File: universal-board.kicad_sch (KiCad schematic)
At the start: 48 parts, among them J1 USB_C_Receptacle, J2 Conn_02x04_Odd_Even, J3 Conn_01x08, J4 CONN_WS2812, J5 CONN_I2C_GROVE, J6 CONN_UART, Q1 BSS138, SW1 SW_RESET, SW2 SW_ACK, U1 USBLC6-2SC6, U2 AMS1117-3.3, U3 CH224K, U4 USBLC6-2SC6, U5 74AHCT1G125, U6 TSOP384xx, U7 ESP32-S3-WROOM-1-N16

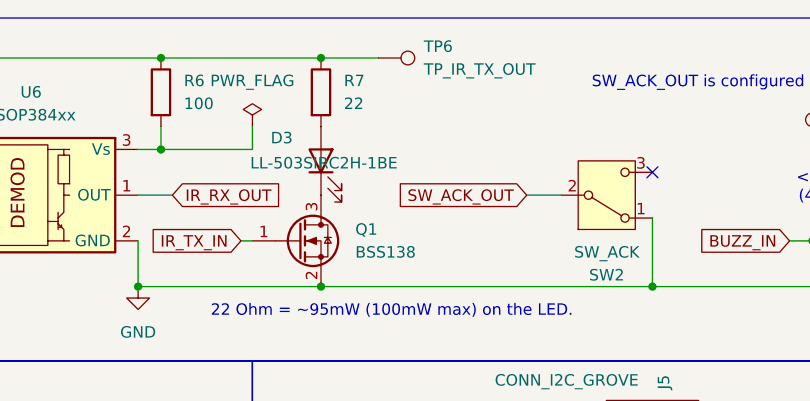
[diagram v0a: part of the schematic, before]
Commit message: PCB is routed, but needs more work.
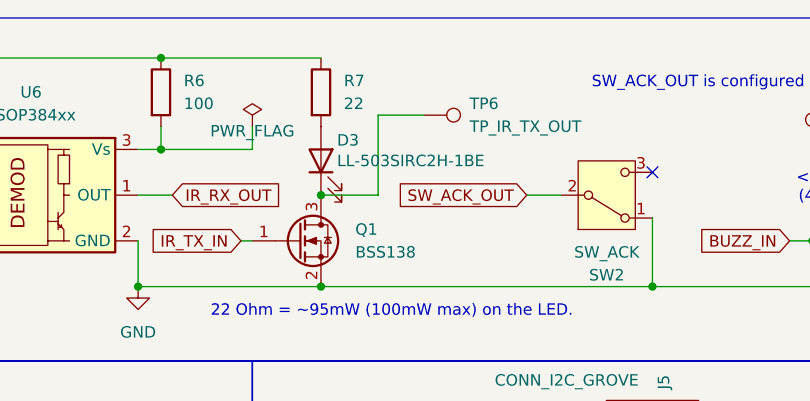
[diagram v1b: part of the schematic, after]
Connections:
- net 3.3V: no longer TP6.1
- net at D3.1 (K), Q1.3 (D): now also TP6.1
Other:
- moved on the sheet: TP6
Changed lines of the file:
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@@
 	)
 	(junction
+		(at 199.39 31.75)
+		(diameter 0)
+		(color 0 0 0 0)
+	)
+	(junction
 		(at 59.69 190.5)
 		(diameter 0)
@@
 	)
 	(junction
-		(at 199.39 16.51)
-		(diameter 0)
-		(color 0 0 0 0)
-	)
-	(junction
 		(at 46.99 190.5)
 		(diameter 0)
@@
 	(wire
 		(pts
+			(xy 205.74 22.86) (xy 210.82 22.86)
+		)
+		(stroke
+			(width 0)
+			(type default)
+		)
+	)
+	(wire
+		(pts
 			(xy 260.35 82.55) (xy 260.35 99.06)
 		)
@@
 	(wire
 		(pts
-			(xy 199.39 16.51) (xy 205.74 16.51)
-		)
-		(stroke
-			(width 0)
-			(type default)
-		)
-	)
-	(wire
-		(pts
 			(xy 97.79 121.92) (xy 135.89 121.92)
 		)
@@
 	(wire
 		(pts
+			(xy 205.74 31.75) (xy 199.39 31.75)
+		)
+		(stroke
+			(width 0)
+			(type default)
+		)
+	)
+	(wire
+		(pts
 			(xy 127 90.17) (xy 114.3 90.17)
 		)
@@
 	(wire
 		(pts
+			(xy 205.74 22.86) (xy 205.74 31.75)
+		)
+		(stroke
+			(width 0)
+			(type default)
+		)
+	)
+	(wire
+		(pts
 			(xy 171.45 63.5) (xy 154.94 63.5)
 		)
@@
 		(on_board yes)
 		(dnp no)
-		(fields_autoplaced yes)
 		(property "Reference" "#FLG04"
 			(at 191.77 22.225 0)
@@
 		)
 		(property "Value" "PWR_FLAG"
-			(at 191.77 19.05 0)
+			(at 191.77 24.638 0)
 			(effects
 				(font
@@
 		(dnp no)
 		(property "Reference" "D3"
-			(at 193.802 25.4 90)
+			(at 201.168 25.654 90)
 			(effects
 				(font
@@
 		)
 		(property "Value" "LL-503SIRC2H-1BE"
-			(at 191.516 28.194 90)
+			(at 201.168 27.94 90)
 			(effects
 				(font
@@
 	(symbol
 		(lib_id "Connector:TestPoint")
-		(at 205.74 16.51 270)
+		(at 210.82 22.86 270)
 		(unit 1)
 		(exclude_from_sim no)
@@
 		(fields_autoplaced yes)
 		(property "Reference" "TP6"
-			(at 210.82 15.2399 90)
+			(at 215.9 21.5899 90)
 			(effects
 				(font
@@
 		)
 		(property "Value" "TP_IR_TX_OUT"
-			(at 210.82 17.7799 90)
+			(at 215.9 24.1299 90)
 			(effects
 				(font
@@
 		)
 		(property "Footprint" "TestPoint:TestPoint_Pad_D2.0mm"
-			(at 205.74 21.59 0)
+			(at 210.82 27.94 0)
 			(effects
 				(font
@@
 		)
 		(property "Datasheet" "~"
-			(at 205.74 21.59 0)
+			(at 210.82 27.94 0)
 			(effects
 				(font
@@
 		)
 		(property "Description" "test point"
-			(at 205.74 16.51 0)
+			(at 210.82 22.86 0)
 			(effects
 				(font

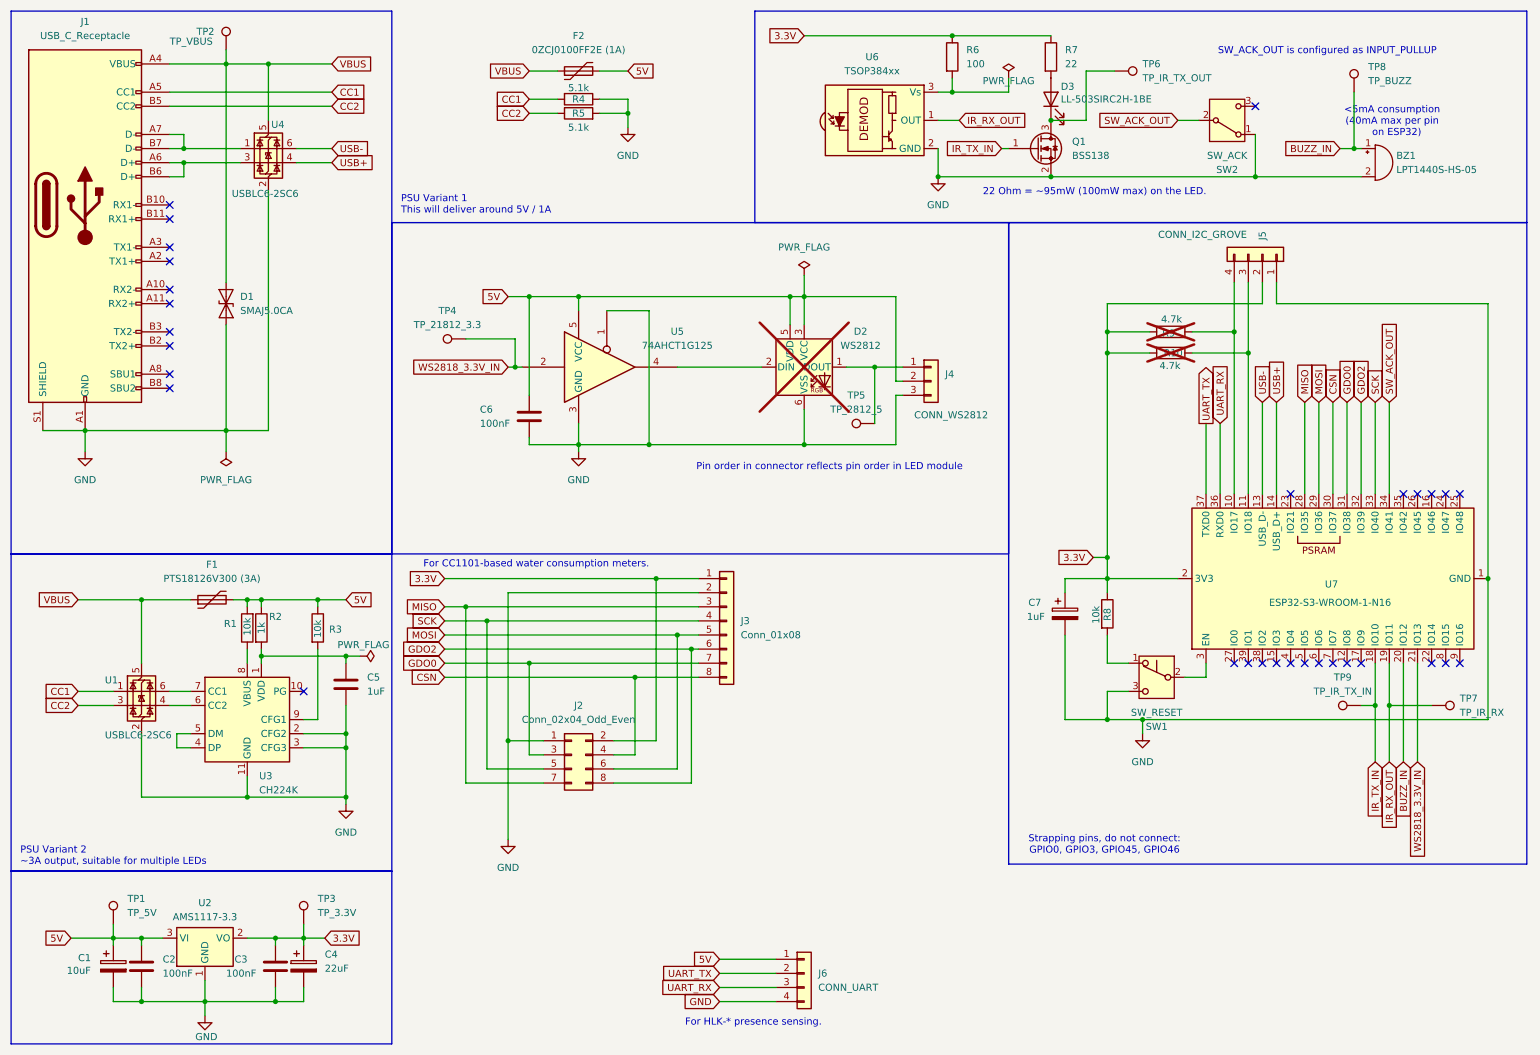
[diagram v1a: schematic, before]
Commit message: Prep for rev 3:
- removed 3A PSU
- added 2 33 ohm resistors for USB
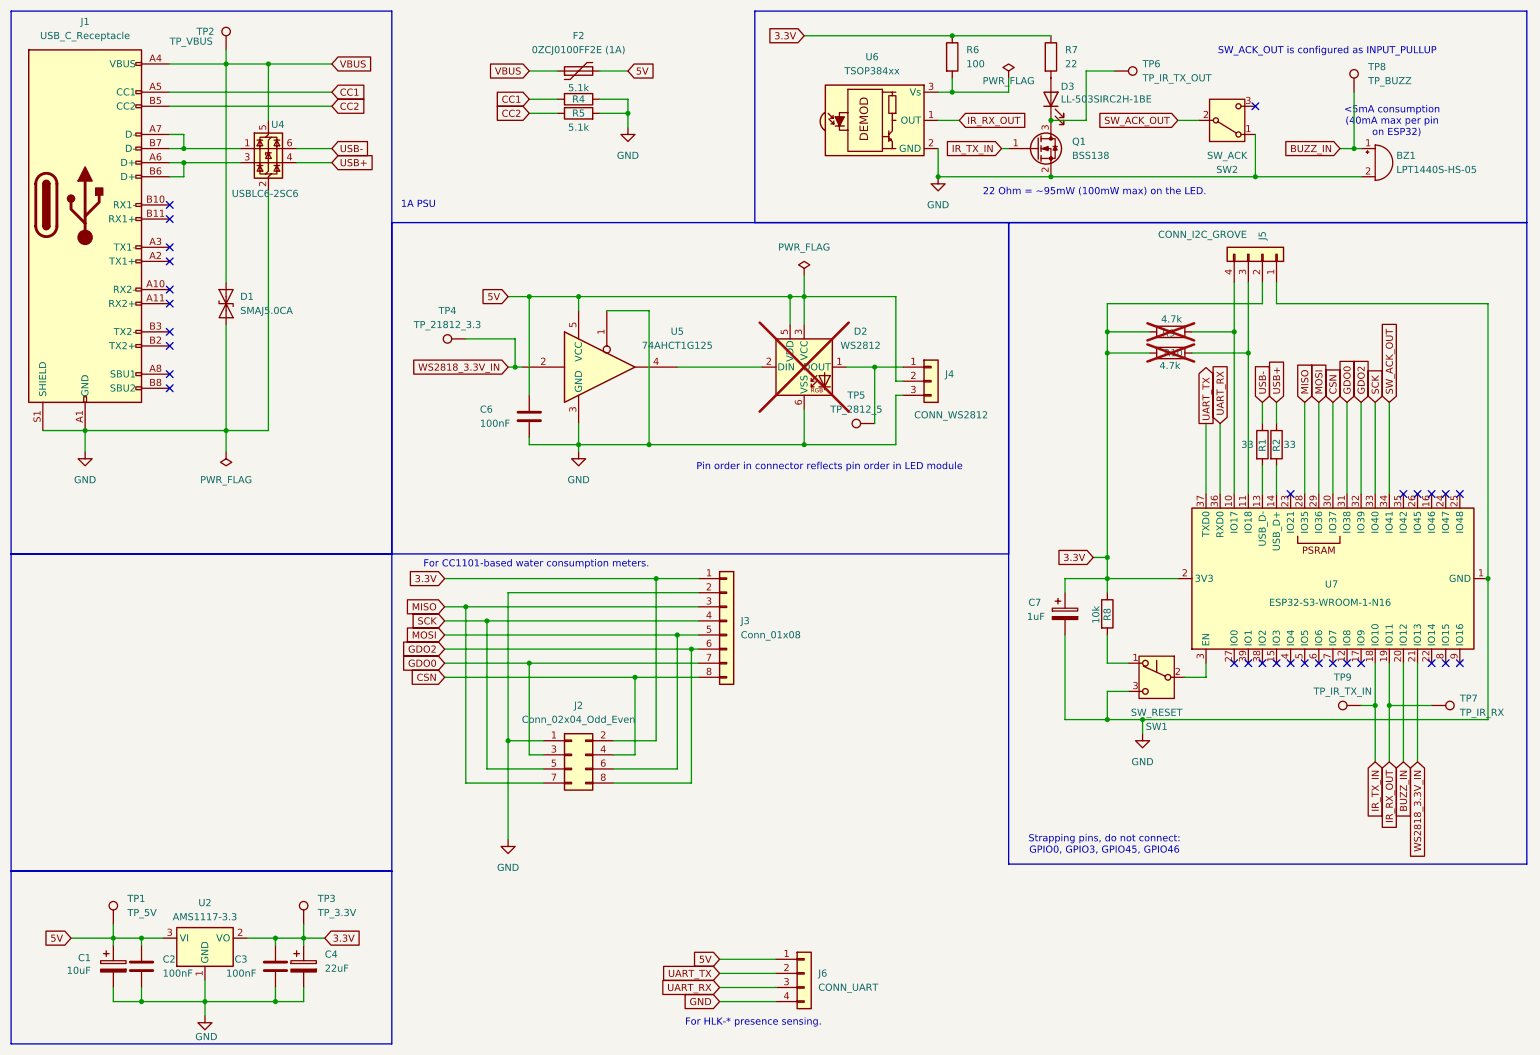
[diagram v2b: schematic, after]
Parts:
- removed C5: 1uF, Capacitor_SMD:C_1206_3216Metric_Pad1.33x1.80mm_HandSolder, symbol Device:C
- removed F1: PTS18126V300 (3A), Fuse:Fuse_1812_4532Metric_Pad1.30x3.40mm_HandSolder, symbol Device:Polyfuse
- removed R3: 10k, Resistor_SMD:R_1206_3216Metric_Pad1.30x1.75mm_HandSolder, symbol Device:R
- removed U1: USBLC6-2SC6, Package_TO_SOT_SMD:SOT-23-6, symbol Power_Protection:USBLC6-2SC6
- removed U3: CH224K, Package_SO:SSOP-10-1EP_3.9x4.9mm_P1mm_EP2.1x3.3mm, symbol Interface_USB:CH224K
- R1: value 10k -> 33; footprint Resistor_SMD:R_1206_3216Metric_Pad1.30x1.75mm_HandSolder -> (none)
- R2: value 1k -> 33; footprint Resistor_SMD:R_1206_3216Metric_Pad1.30x1.75mm_HandSolder -> (none)
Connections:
- net 5V: no longer R1.2, R2.1
- net USB+: now also R2.1; no longer U7.14 (USB_D+)
- net USB-: now also R1.1; no longer U7.13 (USB_D-)
- net at R2.2: now also U7.14 (USB_D+)
- new net: R1.2, U7.13 (USB_D-)
- no-connect marks 31 -> 30
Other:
- note added: "1A PSU"
- note removed: "PSU Variant 1 This will deliver around 5V / 1A"
- note removed: "PSU Variant 2 ~3A output, suitable for multiple LEDs"

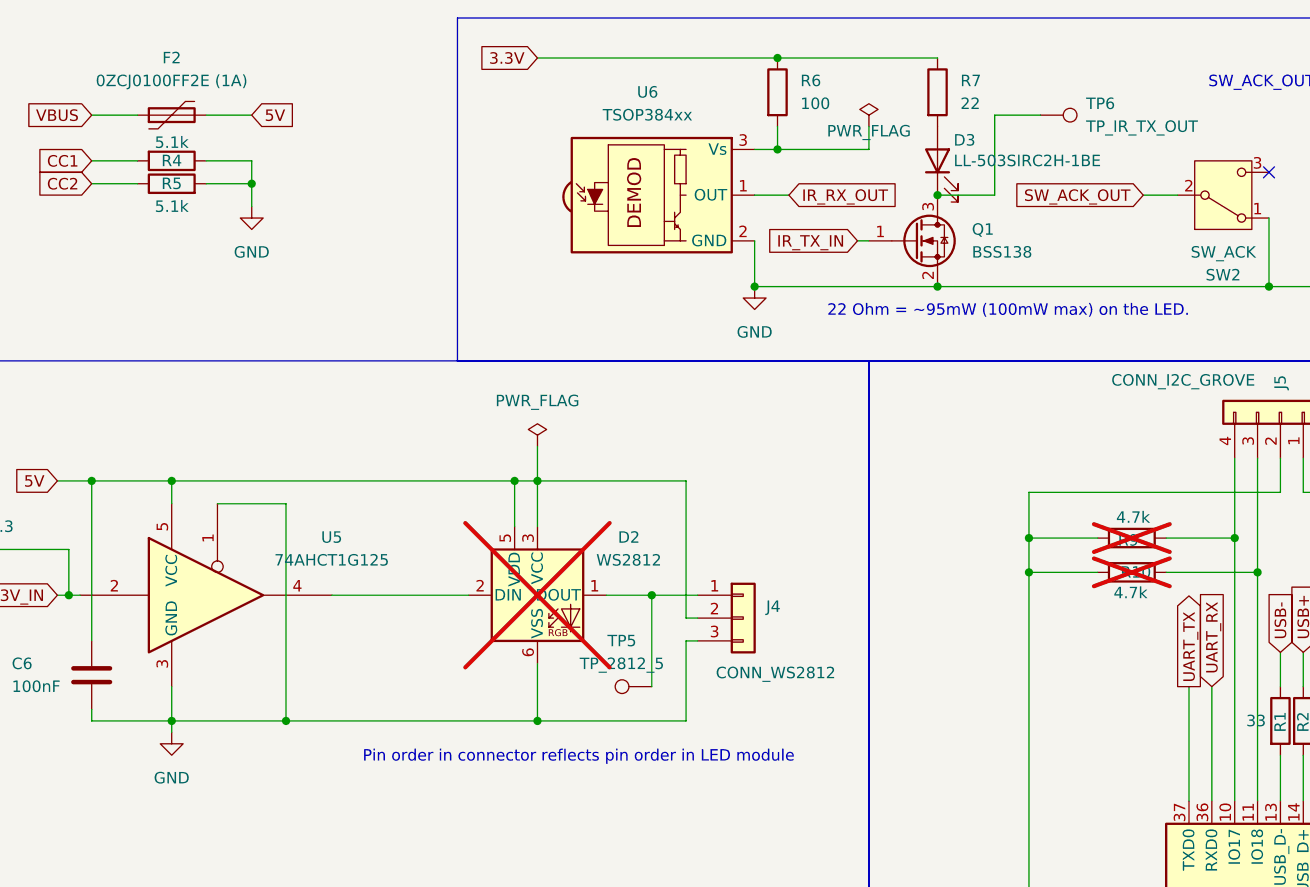
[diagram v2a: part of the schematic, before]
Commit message: Added reference designs for ESP32 modules.
Adjusted IR LED part number.

Added another WS2812.
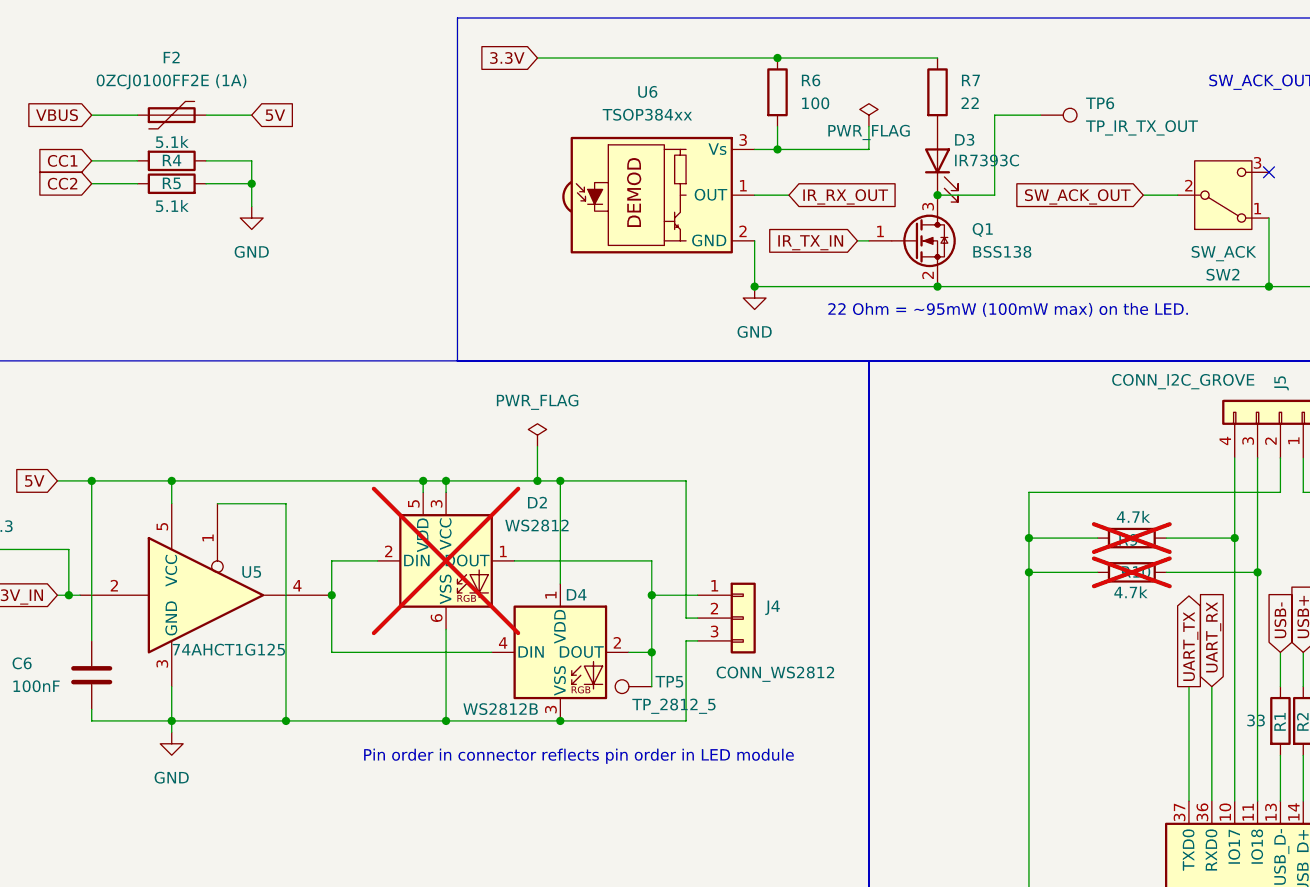
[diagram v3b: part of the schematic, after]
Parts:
- added D4: WS2812B, LED_SMD:LED_WS2812B_PLCC4_5.0x5.0mm_P3.2mm, symbol LED:WS2812B
- D3: value LL-503SIRC2H-1BE -> IR7393C
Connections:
- net 5V: now also D4.1 (VDD)
- net GND: now also D4.3 (VSS)
- net at D2.1 (DOUT), J4.1 (Pin_1), TP5.1: now also D4.2 (DOUT)
- net at D2.2 (DIN), U5.4: now also D4.4 (DIN)
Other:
- moved on the sheet: D2
